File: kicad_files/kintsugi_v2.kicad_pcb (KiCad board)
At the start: 2 copper layers, 366.7 x 102 mm, 162 parts, among them J1 Conn_01x04, J2 Conn_01x04, J3 AudioJack4, J4 AudioJack4, SW1 RotaryEncoder_Switch, SW2 SW_Push, U1 ProMicro, U2 MCP23017_SP

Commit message: Rearranged some components.
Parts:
- J1, J2: moved to B.Cu
- moved J2 85.8 mm to (27.3, 59.9), turned to -90 degrees
- moved C1 44.6 mm to (27.3, 99.2), turned to 0 degrees
- moved R1 38.7 mm to (31.1, 99.2), turned to 0 degrees
- moved C2 29.5 mm to (34.9, 99.2)
- moved U2 29.4 mm to (34.9, 63.5)
- moved D30 28.0 mm to (385.2, 118.9)
- moved SW1 27.9 mm to (382.7, 101.2)
- moved SW2 5.36 mm to (385.2, 41.2)
- moved U1 5.36 mm to (385.2, 50.5)
- moved J1 4.98 mm to (389.0, 69.1), turned to 90 degrees
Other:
- board size 366.7 x 102 mm -> 374.9 x 101.9 mm

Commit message: Routed sockets pads to diodes. Pending review.
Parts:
- added S1: MX_stab, marbastlib-mx:STAB_MX_ISO_FLIPPED, B.Cu at (68.3, 70.6)
- added S2: MX_stab, marbastlib-mx:STAB_MX_2.25u, B.Cu at (77.8, 80.2)
- MX30: footprint acheron_MXH_metalrings:MX150H -> acheron_MXH_metalrings:MX100H
- MX45: footprint acheron_MXH_metalrings:MX225H -> acheron_MXH_metalrings:MX100H
- MX46: footprint acheron_MXH_metalrings:MX_ISOEnterH -> acheron_MXH_metalrings:MX100H
- moved D43 2.03 mm to (84.6, 89.3)
- turned MX30 to 90 degrees
- turned MX44 to -90 degrees
- turned MX45 to -90 degrees
- turned MX46 to -90 degrees
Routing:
- net Net-(D15-Pad2): track 0.00 -> 57.6 mm
- net Net-(D31-Pad2): track 0.00 -> 23.0 mm
- net Net-(D45-Pad2): track 0.00 -> 19.6 mm
- net Net-(D44-Pad2): track 0.00 -> 19.0 mm
- net Net-(D29-Pad2): track 0.00 -> 18.8 mm
- net Net-(D65-Pad2): track 0.00 -> 12.8 mm
- net Net-(D36-Pad2): track 0.00 -> 12.8 mm
- net Net-(D52-Pad2): track 0.00 -> 12.8 mm
- net Net-(D51-Pad2): track 0.00 -> 12.8 mm
- net Net-(D40-Pad2): track 0.00 -> 12.8 mm
- net Net-(D42-Pad2): track 0.00 -> 12.8 mm
- net Net-(D73-Pad2): track 0.00 -> 12.8 mm
- net Net-(D56-Pad2): track 0.00 -> 12.8 mm
- net Net-(D55-Pad2): track 0.00 -> 12.8 mm
- net Net-(D54-Pad2): track 0.00 -> 12.8 mm
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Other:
- board text added: "Fillet R4 = 1.3"
- board text added: "MCP23017"

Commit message: Routed rows of the switch matrix.
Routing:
- net ROW2: track 0.00 -> 174.0 mm
- net ROW10: track 0.00 -> 160.3 mm
- net ROW9: track 0.00 -> 157.9 mm
- net ROW6: track 0.00 -> 143.0 mm
- net ROW8: track 0.00 -> 142.5 mm
- net ROW7: track 0.00 -> 139.6 mm
- net ROW3: track 0.00 -> 134.8 mm
- net ROW0: track 0.00 -> 122.9 mm
- net ROW1: track 0.00 -> 107.3 mm
- net ROW11: track 0.00 -> 71.7 mm
- net ROW5: track 0.00 -> 64.9 mm
- net ROW4: track 0.00 -> 54.3 mm, vias 0 -> 2
- net Net-(D73-Pad2): track 12.8 -> 13.9 mm
- net Net-(D72-Pad2): track 12.8 -> 13.9 mm
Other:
- board text added: "Fillet diodes = 1.3 Fillet rows = 2"
- board text removed: "Fillet R4 = 1.3"

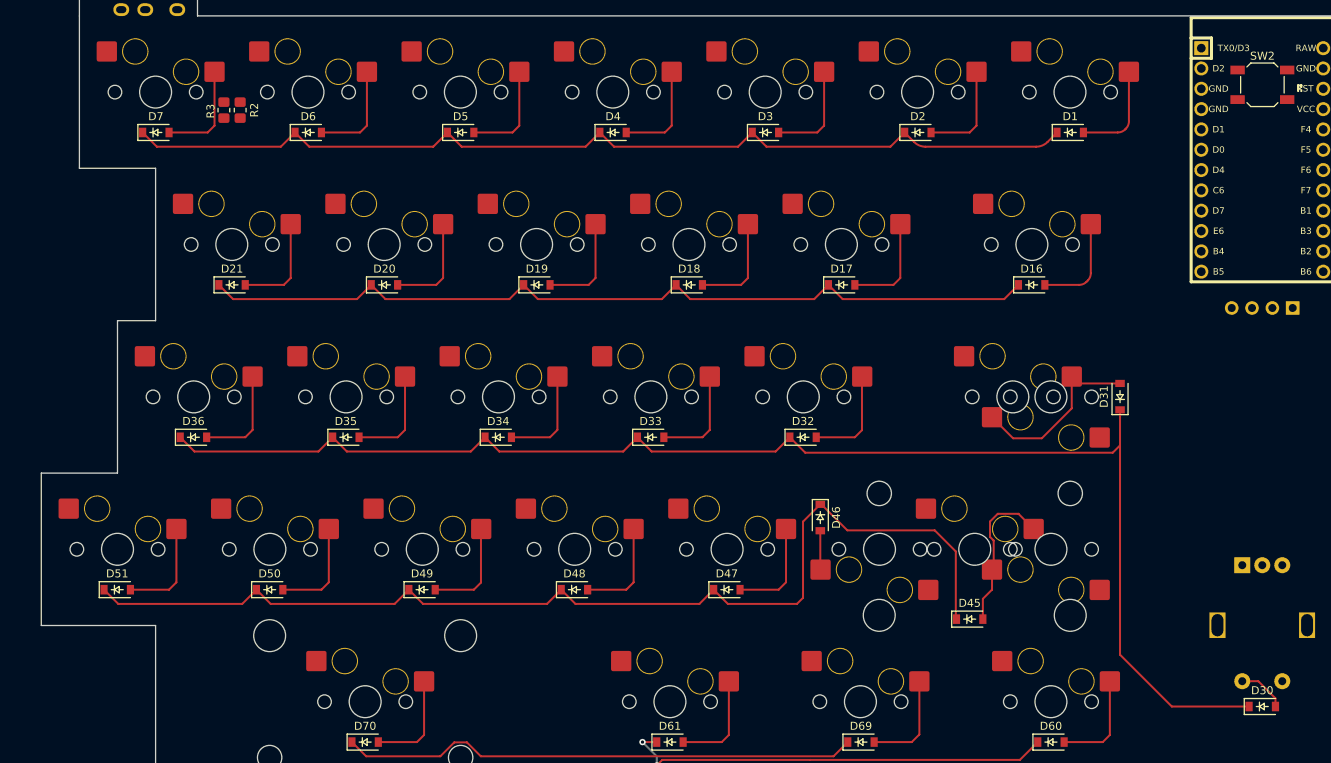
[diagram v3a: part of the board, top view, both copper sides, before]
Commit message: Routed cols of the right side (down view) of the keyboard.
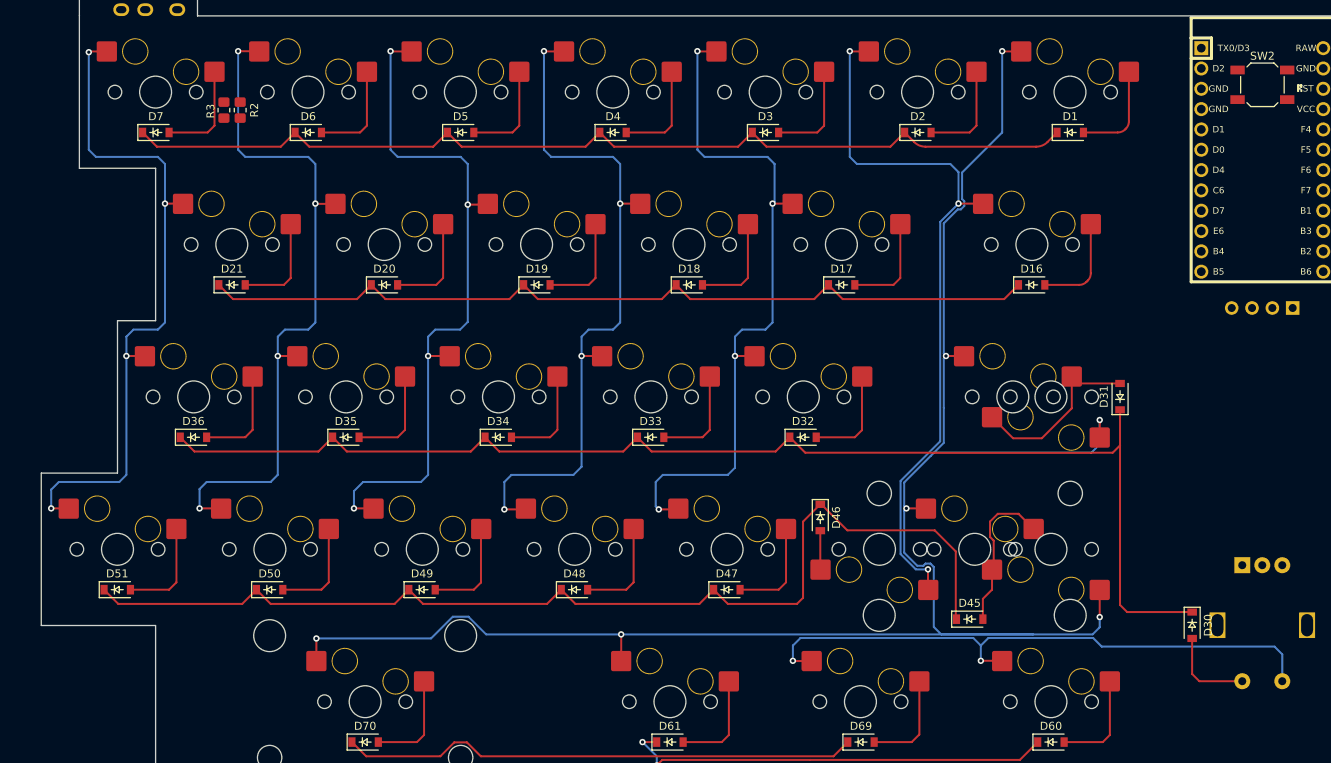
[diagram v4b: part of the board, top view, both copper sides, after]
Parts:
- moved D30 13.4 mm to (376.4, 108.7), turned to -90 degrees
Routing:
- net COL1: track 0.00 -> 238.3 mm, vias 0 -> 7
- net COL2: track 0.00 -> 90.6 mm, vias 0 -> 3
- net COL3: track 0.00 -> 88.5 mm, vias 0 -> 4
- net COL6: track 0.00 -> 88.5 mm, vias 0 -> 4
- net COL4: track 0.00 -> 88.4 mm, vias 0 -> 4
- net COL5: track 0.00 -> 88.1 mm, vias 0 -> 4
- net COL7: track 0.00 -> 86.7 mm, vias 0 -> 4
- net COL0: track 0.00 -> 75.4 mm, vias 0 -> 2
- net ROW2: track 174.0 -> 158.3 mm
- net RE: track 6.06 -> 11.1 mm

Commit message: Routed rows of the right side (down view) to the MCU.
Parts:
- moved D30 1.78 mm to (374.6, 108.7)
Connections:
- U1 pad 1: COL6 -> ROW0
- U1 pad 10: ROW3 -> ROW4
- U1 pad 11: ENCA -> ENCB
- U1 pad 12: ENCB -> ENCA
- U1 pad 13: ROW4 -> COL6
- U1 pad 14: ROW5 -> COL7
- U1 pad 2: COL7 -> ROW1
- U1 pad 7: ROW0 -> ROW2
- U1 pad 8: ROW1 -> ROW3
- U1 pad 9: ROW2 -> ROW5
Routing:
- net ROW5: track 64.9 -> 189.1 mm
- net ROW4: track 54.3 -> 157.6 mm
- net ROW3: track 134.8 -> 232.6 mm
- net ENCB: track 0.00 -> 68.0 mm
- net ENCA: track 0.00 -> 62.7 mm
- net ROW1: track 107.3 -> 160.0 mm
- net ROW2: track 158.3 -> 193.0 mm
- net SDA0: track 0.00 -> 31.0 mm
- net ROW0: track 122.9 -> 152.7 mm
- net SCL0: track 0.00 -> 29.4 mm
- net GND: track 0.00 -> 18.8 mm
- net RESET: track 0.00 -> 11.3 mm
- net RE: track 11.1 -> 12.9 mm

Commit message: Filleted edge cuts.
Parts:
- U1: moved to B.Cu
- moved SW2 0.14 mm to (385.2, 41.0)
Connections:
- U1 pad 10: ROW4 -> COL5
- U1 pad 11: ENCB -> COL6
- U1 pad 12: ENCA -> COL7
- U1 pad 13: COL6 -> COL2
- U1 pad 14: COL7 -> COL1
- U1 pad 15: COL0 -> ENCA
- U1 pad 16: COL1 -> ENCB
- U1 pad 17: COL2 -> ROW4
- U1 pad 18: COL3 -> ROW5
- U1 pad 19: COL4 -> ROW3
- U1 pad 20: COL5 -> ROW2
- U1 pad 7: ROW2 -> COL0
- U1 pad 8: ROW3 -> COL3
- U1 pad 9: ROW5 -> COL4
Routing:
- net VCC: track 0.00 -> 192.5 mm, vias 0 -> 1
- net SDA0: track 31.0 -> 213.8 mm, vias 0 -> 1
- net SCL0: track 29.4 -> 210.2 mm
- net COL7: track 86.7 -> 246.7 mm, vias 4 -> 5
- net COL6: track 88.5 -> 237.2 mm, vias 4 -> 5
- net COL5: track 88.1 -> 222.0 mm, vias 4 -> 5
- net COL4: track 88.4 -> 206.2 mm, vias 4 -> 5
- net COL3: track 88.5 -> 190.1 mm, vias 4 -> 5
- net GND: track 18.8 -> 88.1 mm
- net COL0: track 75.4 -> 141.2 mm
- net COL2: track 90.6 -> 131.6 mm, vias 3 -> 4
- net COL1: track 238.3 -> 276.2 mm
- net ROW0: track 152.7 -> 170.1 mm
- net ROW1: track 160.0 -> 176.6 mm
- net ROW2: track 193.0 -> 198.6 mm
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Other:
- board size 374.9 x 101.9 mm -> 374.9 x 101.5 mm

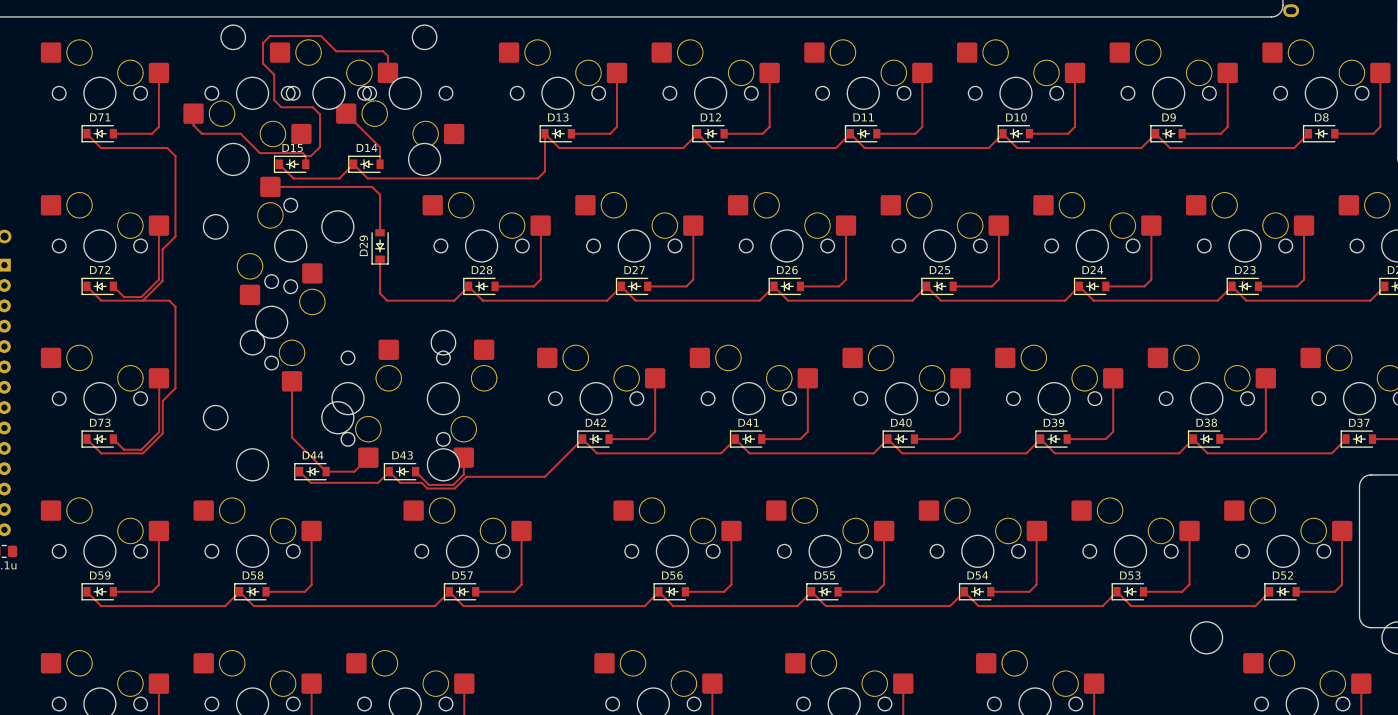
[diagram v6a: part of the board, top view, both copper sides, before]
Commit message: Routed rows of the left side (down view) of the keyboard.
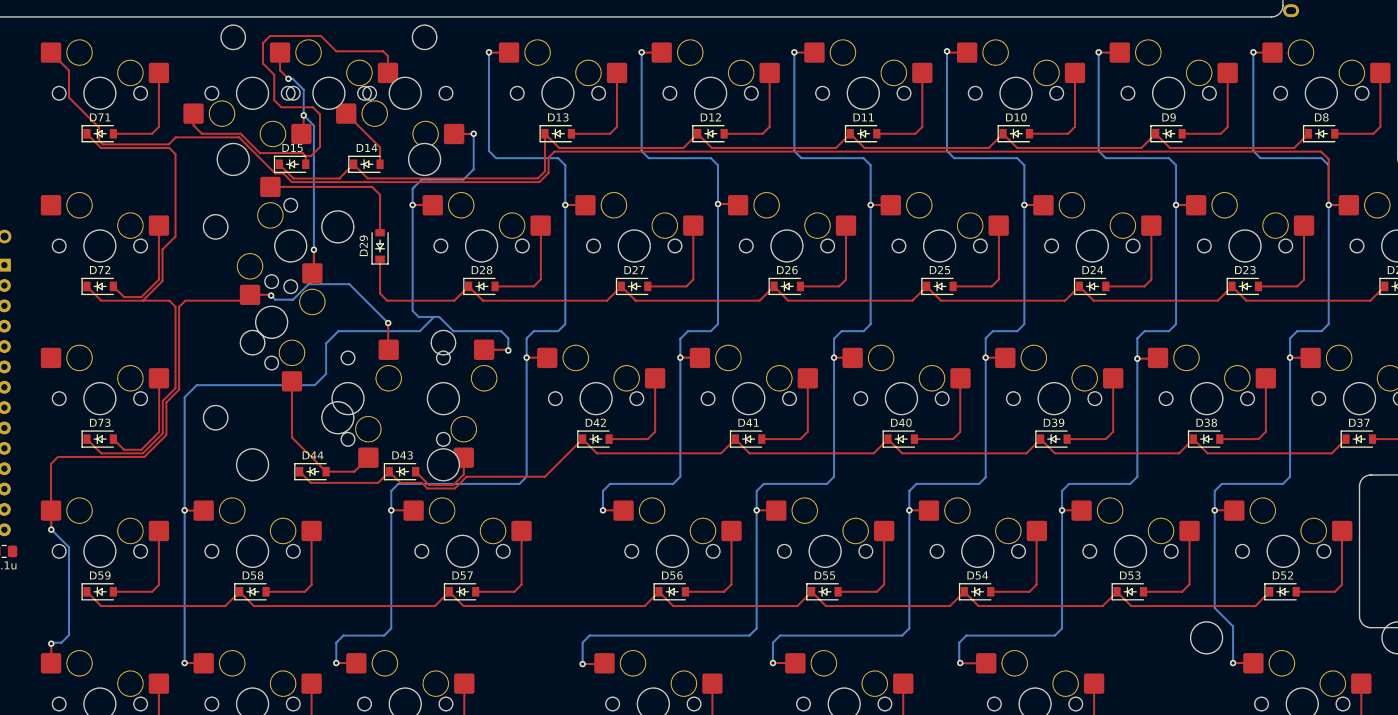
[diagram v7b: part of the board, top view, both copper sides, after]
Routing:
- net COL8: track 0.00 -> 288.7 mm, vias 0 -> 5
- net COL11: track 0.00 -> 130.2 mm, vias 0 -> 5
- net COL15: track 0.00 -> 129.8 mm, vias 0 -> 7
- net COL14: track 0.00 -> 126.7 mm, vias 0 -> 5
- net COL10: track 0.00 -> 125.9 mm, vias 0 -> 5
- net COL13: track 0.00 -> 123.1 mm, vias 0 -> 5
- net COL9: track 0.00 -> 122.3 mm, vias 0 -> 5
- net COL12: track 0.00 -> 88.0 mm, vias 0 -> 4

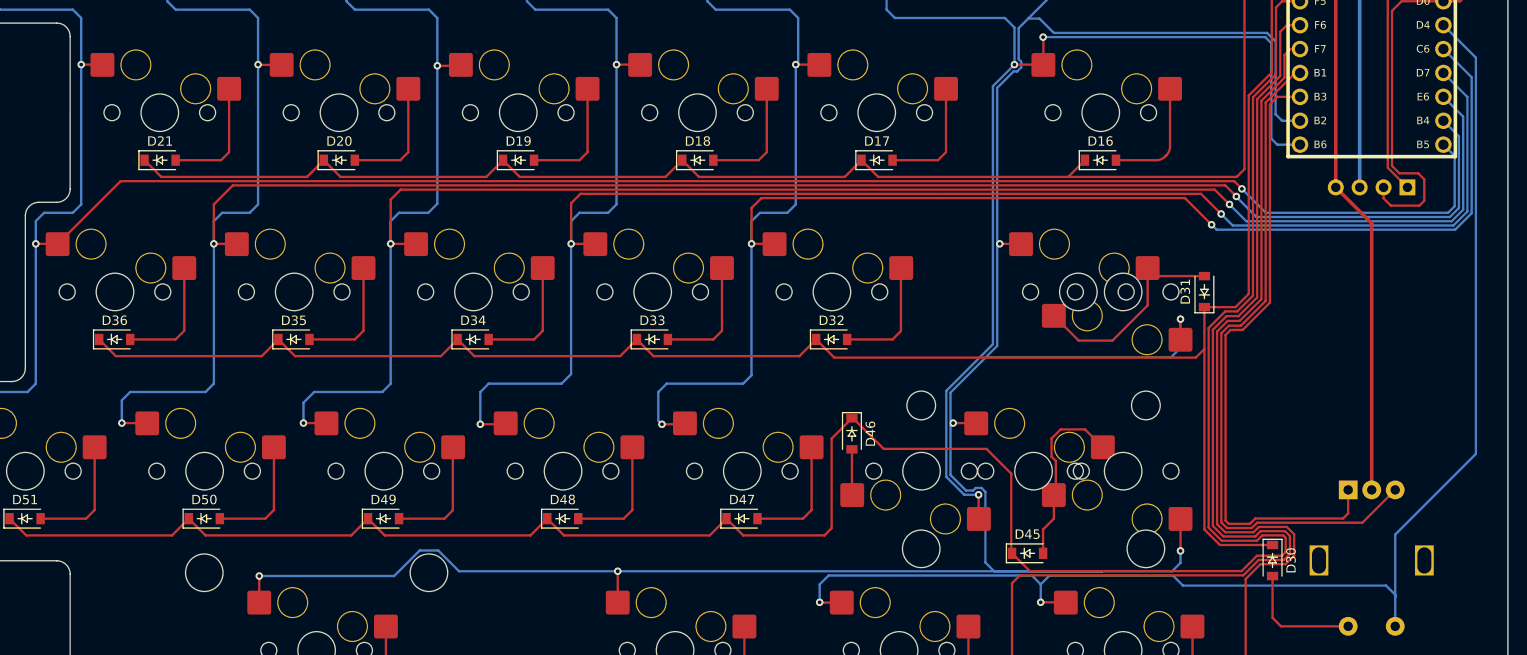
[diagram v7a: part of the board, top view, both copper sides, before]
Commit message: Re-arranged some traces.
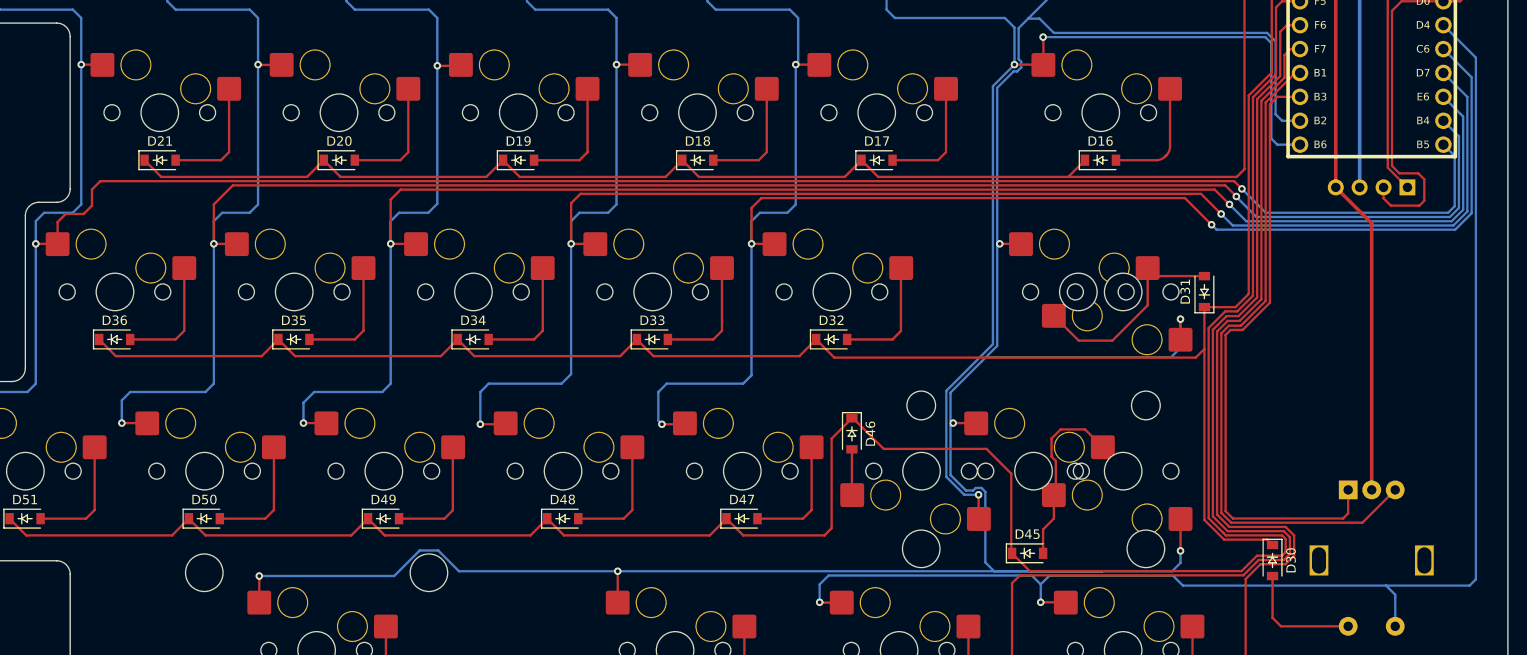
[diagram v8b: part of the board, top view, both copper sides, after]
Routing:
- net COL0: track 141.2 -> 145.6 mm
- net COL7: track 246.7 -> 249.1 mm
- net ROW3: track 237.9 -> 236.8 mm
- net ROW5: track 193.1 -> 192.0 mm
- net ROW4: track 158.5 -> 157.3 mm
- net ENCB: track 72.7 -> 71.6 mm
- net ENCA: track 66.6 -> 65.5 mm
- net ROW2: track 198.6 -> 198.0 mm
